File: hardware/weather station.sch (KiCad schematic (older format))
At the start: 20 parts, among them P1 DC MOTOR, P2 TO MAIN BOARD, U1 LM324

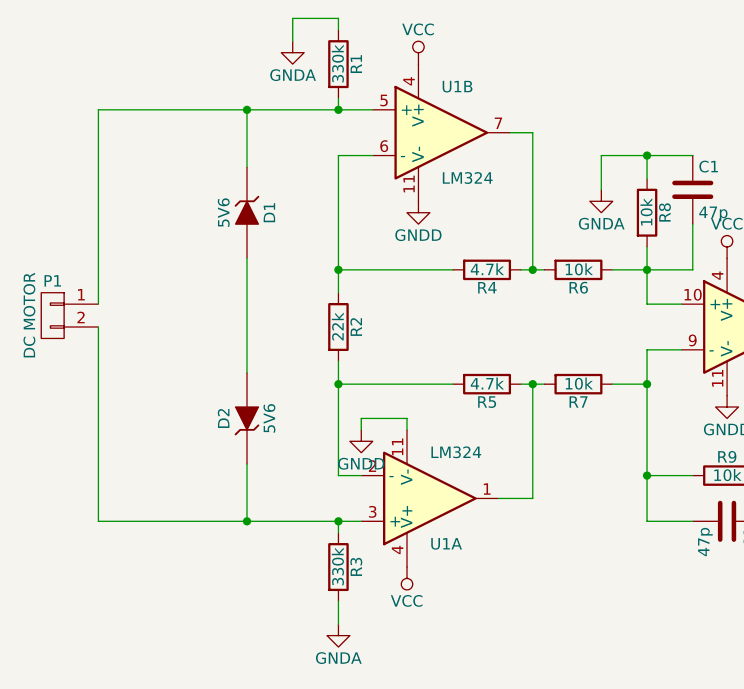
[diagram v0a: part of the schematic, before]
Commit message: Anemometer: modify input R for instr amp
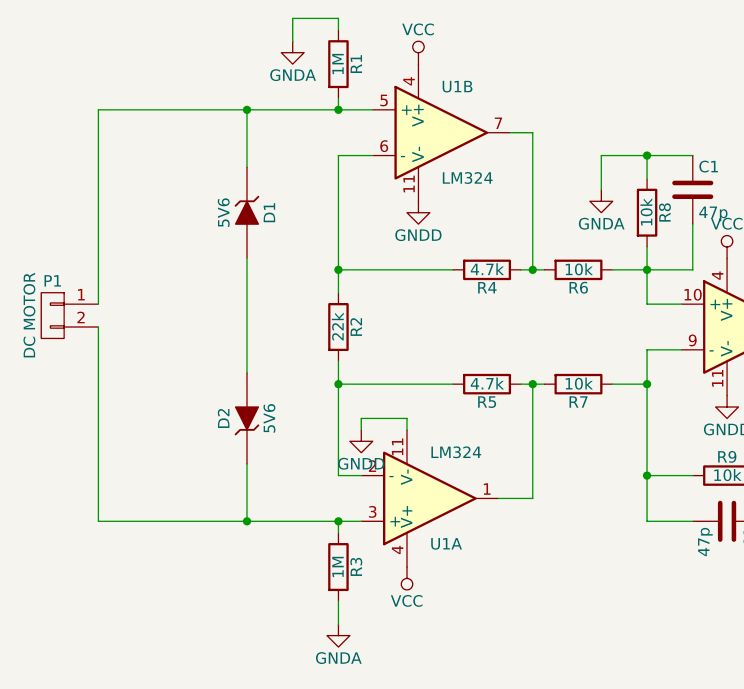
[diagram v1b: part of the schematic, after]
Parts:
- R1, R3: value 330k -> 1M
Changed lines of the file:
@@
 P 4050 1950
 F 0 "R1" V 4130 1950 50  0000 C CNN
-F 1 "330k" V 4050 1950 50  0000 C CNN
+F 1 "1M" V 4050 1950 50  0000 C CNN
 F 2 "" V 3980 1950 50  0000 C CNN
 F 3 "" H 4050 1950 50  0000 C CNN
@@
 P 4050 4150
 F 0 "R3" V 4130 4150 50  0000 C CNN
-F 1 "330k" V 4050 4150 50  0000 C CNN
+F 1 "1M" V 4050 4150 50  0000 C CNN
 F 2 "" V 3980 4150 50  0000 C CNN
 F 3 "" H 4050 4150 50  0000 C CNN

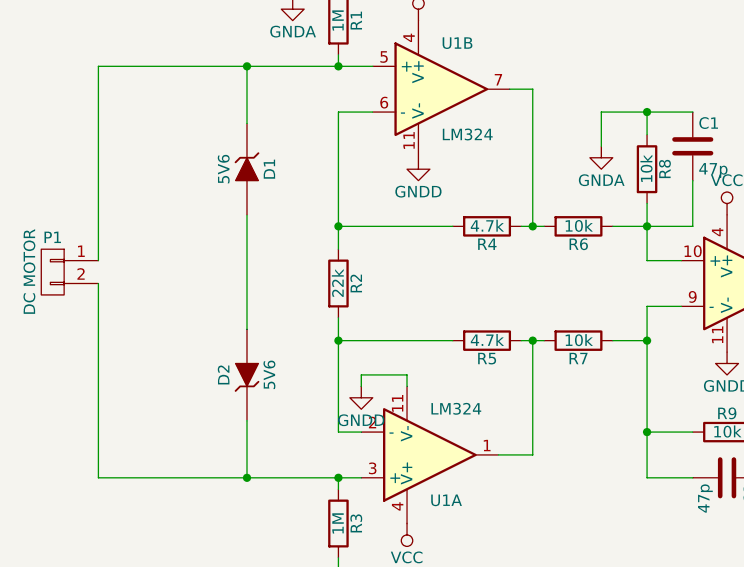
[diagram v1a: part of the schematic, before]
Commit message: add calibration parameters for anemometer
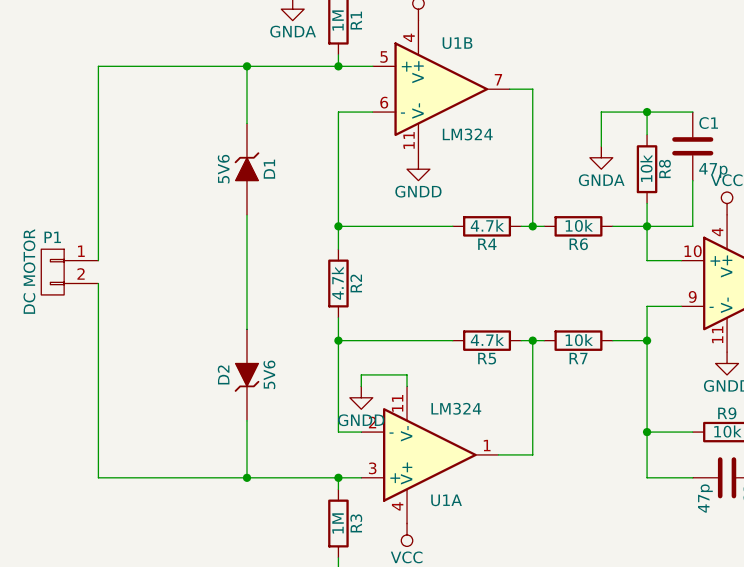
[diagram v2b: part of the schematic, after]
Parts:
- R2: value 22k -> 4.7k
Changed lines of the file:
@@
 P 4050 3100
 F 0 "R2" V 4130 3100 50  0000 C CNN
-F 1 "22k" V 4050 3100 50  0000 C CNN
+F 1 "4.7k" V 4050 3100 50  0000 C CNN
 F 2 "" V 3980 3100 50  0000 C CNN
 F 3 "" H 4050 3100 50  0000 C CNN

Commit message: WIP: adding HW resources
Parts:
- removed C1, C2: 47p, symbol C
- removed C3, C4: 0.1u, symbol C
- removed D1, D2: 5V6, symbol ZENER
- removed P1: DC MOTOR, symbol CONN_01X02
- removed P2: TO MAIN BOARD, symbol CONN_01X05
- removed R1, R3: 1M, symbol R
- removed R10, R11: 15k, symbol R
- removed R2, R4, R5: 4.7k, symbol R
- removed R6, R7, R8, R9: 10k, symbol R
- removed U1: LM324, symbol LM324
- added C1, C13, C6: 220u, Capacitor_SMD:CP_Elec_8x10.5, symbol Device:CP
- added C10, C11, C12, C2, C5, C8, C9: .1u, Capacitor_SMD:C_0805_2012Metric_Pad1.15x1.40mm_HandSolder, symbol Device:C
- added C3, C4, C7: 1u, Capacitor_SMD:C_0805_2012Metric_Pad1.15x1.40mm_HandSolder, symbol Device:C
- added D1, D2, D4, D5: D, Diode_SMD:D_SMB_Handsoldering, symbol Device:D
- added D3: LED, LED_SMD:LED_1206_3216Metric_Pad1.42x1.75mm_HandSolder, symbol Device:LED
- added J1: Conn_01x05, Connector_PinHeader_2.54mm:PinHeader_1x05_P2.54mm_Vertical, symbol Connector_Generic:Conn_01x05
- added J10: Pressure, Connector_PinHeader_2.54mm:PinHeader_1x06_P2.54mm_Vertical, symbol Connector_Generic:Conn_01x06
- added J11: Conn_01x04, Connector_PinHeader_2.54mm:PinHeader_1x04_P2.54mm_Vertical, symbol Connector_Generic:Conn_01x04
- added J12: Conn_02x07_Odd_Even, Connector_PinSocket_2.00mm:PinSocket_2x07_P2.00mm_Vertical, symbol Connector_Generic:Conn_02x07_Odd_Even
- added J2: DIG_EXP, Connector_PinHeader_2.54mm:PinHeader_1x06_P2.54mm_Vertical, symbol Connector_Generic:Conn_01x06
- added J3: ICSP, Connector_PinHeader_2.54mm:PinHeader_1x05_P2.54mm_Vertical, symbol Connector_Generic:Conn_01x05
- added J4: BAT., TerminalBlock_4Ucon:TerminalBlock_4Ucon_1x02_P3.50mm_Horizontal, symbol Connector:Conn_01x02_Female
- added J5: EXP0, Connector_PinHeader_2.54mm:PinHeader_1x04_P2.54mm_Vertical, symbol Connector_Generic:Conn_01x04
- added J6: EXP1, Connector_PinHeader_2.54mm:PinHeader_1x04_P2.54mm_Vertical, symbol Connector_Generic:Conn_01x04
- added J7: Wind, Connector_PinHeader_2.54mm:PinHeader_1x05_P2.54mm_Vertical, symbol Connector_Generic:Conn_01x05
- added J8: Conn_01x08, Connector_PinHeader_2.54mm:PinHeader_1x08_P2.54mm_Vertical, symbol Connector_Generic:Conn_01x08
- added J9: HMC5883L, Connector_PinHeader_2.54mm:PinHeader_1x05_P2.54mm_Vertical, symbol Connector_Generic:Conn_01x05
- added R1: 680R, Resistor_SMD:R_0805_2012Metric_Pad1.15x1.40mm_HandSolder, symbol Device:R
- added R10, R6: 100k, Resistor_SMD:R_0805_2012Metric_Pad1.15x1.40mm_HandSolder, symbol Device:R
- added R11, R12: 1M, Resistor_SMD:R_0805_2012Metric_Pad1.15x1.40mm_HandSolder, symbol Device:R
- added R13, R14, R15, R16, R17: 0R, Resistor_SMD:R_0805_2012Metric_Pad1.15x1.40mm_HandSolder, symbol Device:R
- added R2: 10K, Resistor_SMD:R_0805_2012Metric_Pad1.15x1.40mm_HandSolder, symbol Device:R
- added R3, R5: 4k7, Resistor_SMD:R_0805_2012Metric_Pad1.15x1.40mm_HandSolder, symbol Device:R
- added R4, R8, R9: 100R, Resistor_SMD:R_0805_2012Metric_Pad1.15x1.40mm_HandSolder, symbol Device:R
- added R7: 10k, Resistor_SMD:R_0805_2012Metric_Pad1.15x1.40mm_HandSolder, symbol Device:R
- added U1: 18650_CHARGER, modules:TP4056, symbol Taur:18650_CHARGER
- added U2: dsPIC30F4011, Package_DFN_QFN:QFN-44-1EP_8x8mm_P0.65mm_EP6.6x6.6mm, symbol Taur:dsPIC30F4011
- added U3: DC-DC(5V), modules:DM06, symbol Taur:DC-DC(5V)
- added U4: TLE2426xD, Package_SO:SOIC-8_3.9x4.9mm_P1.27mm, symbol Reference_Voltage:TLE2426xD
- added U5, U6: LM2904, Package_SO:TSSOP-8_4.4x3mm_P0.65mm, symbol Amplifier_Operational:LM2904
- added U7: TLV70033_SOT23-5, Package_TO_SOT_SMD:SOT-23-5, symbol Regulator_Linear:TLV70033_SOT23-5
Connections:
- net labels added: +5V, +BATT, AN0, AN1, CTRL0, CTRL1, GND, LED, PGC, PGD, SCL, SDA, SOLAR_PANEL, VGND, WIFI_BOOT, WIFI_EN, WIFI_READY, WIFI_RESET, WIFI_RX, WIFI_TX, WIND
- net labels removed: GNDA, GNDD, VCC
- wire segments 58 -> 261
